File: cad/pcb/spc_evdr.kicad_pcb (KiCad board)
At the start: 2 copper layers, 199.5 x 100.5 mm, 93 parts, among them J1 BL_CONN, SW1 SW_Push, SW10 SW_Push, SW11 SW_Push, SW12 SW_Push, SW13 ON_OFF, SW14 SW_Push, SW15 SW_Push, SW16 SW_Push, SW17 SW_Push, SW18 SW_Push, SW19 SW_Push, SW2 SW_Push, SW20 SW_Push, SW21 SW_Push, SW22 SW_Push, SW23 SW_Push, SW24 SW_Push, SW25 SW_Push, SW26 SW_Push, SW27 SW_Push, SW28 SW_Push, SW29 SW_Push, SW3 SW_Push, SW30 SW_Push, SW31 SW_Push, SW32 SW_Push, SW33 SW_Push, SW34 SW_Push, SW35 SW_Push, SW36 SW_Push, SW37 SW_Push, SW38 SW_Push, SW39 SW_Push, SW4 SW_Push, SW40 SW_Push, SW41 SW_Push, SW42 SW_Push, SW43 SW_Push, SW44 SW_Push, SW45 SW_Push, SW5 RotaryEncoder_Switch, SW6 SW_Push, SW7 SW_Push, SW8 SW_Push, SW9 SW_Push, U1 PCA9555PW, U2 xiao-ble

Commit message: added a whole lot of peripherals
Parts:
- added BZ1: Buzzer, KLOR:Buzzer_Mallory_AST1109MLTRQ_reversible, B.Cu at (85.7, 49.7)
- added D1: D, weteor:D_SOD-123, B.Cu at (48.8, 75.7)
- added D11: D, weteor:D_SOD-123, B.Cu at (222.6, 75.7)
- added D13: D, weteor:D_SOD-123, B.Cu at (48.8, 94.7)
- added D23: D, weteor:D_SOD-123, B.Cu at (222.6, 94.7)
- added D25: D, weteor:D_SOD-123, B.Cu at (48.8, 113.8)
- added D35: D, weteor:D_SOD-123, B.Cu at (222.6, 113.8)
- added D37: D, weteor:D_SOD-123, B.Cu at (48.8, 132.8)
- added D46: D, weteor:D_SOD-123, B.Cu at (231.0, 132.8)
- added D48: ~, weteor:D_SOD-123, F.Cu at (244.0, 131.5)
- added D49: ~, weteor:D_SOD-123, F.Cu at (251.0, 131.5)
- added D50: ~, weteor:D_SOD-123, F.Cu at (255.5, 131.7)
- added D51: ~, weteor:D_SOD-123, F.Cu at (245.0, 115.5)
- added D52: ~, weteor:D_SOD-123, F.Cu at (254.5, 115.5)
- added L1: SK6812MINI, LED_SMD:LED_SK6812MINI_PLCC4_3.5x3.5mm_P1.75mm, F.Cu at (242.1, 47.0)
- added L2: SK6812MINI, LED_SMD:LED_SK6812MINI_PLCC4_3.5x3.5mm_P1.75mm, F.Cu at (250.1, 47.0)
- added L3: SK6812MINI, LED_SMD:LED_SK6812MINI_PLCC4_3.5x3.5mm_P1.75mm, F.Cu at (258.1, 47.0)
- added SW1: SW_Push, weteor:CherryMX_Hotswap, F.Cu at (40.5, 66.2)
- added SW12: SW_Push, weteor:CherryMX_Hotswap, F.Cu at (231.0, 66.2)
- added SW15: SW_Push, weteor:CherryMX_Hotswap, F.Cu at (40.5, 85.2)
- added SW25: SW_Push, weteor:CherryMX_Hotswap, F.Cu at (231.0, 85.2)
- added SW27: SW_Push, weteor:CherryMX_Hotswap, F.Cu at (40.5, 104.3)
- added SW37: SW_Push, weteor:CherryMX_Hotswap, F.Cu at (231.0, 104.3)
- added SW39: SW_Push, weteor:CherryMX_Hotswap, F.Cu at (40.5, 123.3)
- added SW47: SW_Push, weteor:CherryMX_Hotswap, F.Cu at (231.0, 123.3)
- added SW54: SKRHAAE010, mouser:SKRHAAE010, F.Cu at (250.0, 123.3)
- added U3: Pimoroni haptic buzz, KLOR:Pimoroni Haptic Buzz DRV2605L Driver, B.Cu at (202.0, 53.5)
- SW10: renamed from SW35; footprint weteor:Inv1_CherryMX_Hotswap -> weteor:CherryMX_Hotswap
- SW11: renamed from SW38; footprint weteor:Inv1_CherryMX_Hotswap -> weteor:CherryMX_Hotswap
- SW14: renamed from SW42; footprint weteor:Inv1_CherryMX_Hotswap -> weteor:CherryMX_Hotswap
- SW16: renamed from SW2; footprint weteor:Inv1_CherryMX_Hotswap -> weteor:CherryMX_Hotswap
- SW17: renamed from SW7; footprint weteor:Inv1_CherryMX_Hotswap -> weteor:CherryMX_Hotswap
- SW18: renamed from SW11; footprint weteor:Inv1_CherryMX_Hotswap -> weteor:CherryMX_Hotswap
- SW19: renamed from SW15; footprint weteor:Inv1_CherryMX_Hotswap -> weteor:CherryMX_Hotswap
- SW2: renamed from SW1; footprint weteor:Inv1_CherryMX_Hotswap -> weteor:CherryMX_Hotswap
- SW20: renamed from SW21; footprint weteor:Inv1_CherryMX_Hotswap -> weteor:CherryMX_Hotswap
- SW21: renamed from SW26; footprint weteor:Inv1_CherryMX_Hotswap -> weteor:CherryMX_Hotswap
- SW22: renamed from SW32; footprint weteor:Inv1_CherryMX_Hotswap -> weteor:CherryMX_Hotswap
- SW23: renamed from SW36; footprint weteor:Inv1_CherryMX_Hotswap -> weteor:CherryMX_Hotswap
- SW24: renamed from SW39; footprint weteor:Inv1_CherryMX_Hotswap -> weteor:CherryMX_Hotswap
- SW26: renamed from SW43; footprint weteor:Inv1_CherryMX_Hotswap -> weteor:CherryMX_Hotswap
- SW28: renamed from SW3; footprint weteor:Inv1_CherryMX_Hotswap -> weteor:CherryMX_Hotswap
- SW29: renamed from SW8; footprint weteor:Inv1_CherryMX_Hotswap -> weteor:CherryMX_Hotswap
- SW3: renamed from SW6; footprint weteor:Inv1_CherryMX_Hotswap -> weteor:CherryMX_Hotswap
- SW30: renamed from SW12; footprint weteor:Inv1_CherryMX_Hotswap -> weteor:CherryMX_Hotswap
- SW31: renamed from SW16; footprint weteor:Inv1_CherryMX_Hotswap -> weteor:CherryMX_Hotswap
- SW32: renamed from SW22; footprint weteor:Inv1_CherryMX_Hotswap -> weteor:CherryMX_Hotswap
- SW33: renamed from SW27; footprint weteor:Inv1_CherryMX_Hotswap -> weteor:CherryMX_Hotswap
- SW34: renamed from SW33; footprint weteor:Inv1_CherryMX_Hotswap -> weteor:CherryMX_Hotswap
- SW35: renamed from SW37; footprint weteor:Inv1_CherryMX_Hotswap -> weteor:CherryMX_Hotswap
- SW36: renamed from SW40; footprint weteor:Inv1_CherryMX_Hotswap -> weteor:CherryMX_Hotswap
- SW38: renamed from SW44; footprint weteor:Inv1_CherryMX_Hotswap -> weteor:CherryMX_Hotswap
- SW4: renamed from SW10; footprint weteor:Inv1_CherryMX_Hotswap -> weteor:CherryMX_Hotswap
- SW40: renamed from SW4; footprint weteor:Inv1_CherryMX_Hotswap -> weteor:CherryMX_Hotswap
- SW41: renamed from SW9; footprint weteor:Inv1_CherryMX_Hotswap -> weteor:CherryMX_Hotswap
- SW42: renamed from SW17; footprint weteor:Inv1_CherryMX_Hotswap -> weteor:CherryMX_Hotswap
- SW43: renamed from SW23; footprint weteor:Inv_CherryMX_Hotswap_1.75u -> weteor:CherryMX_Hotswap_1.75u
- SW44: renamed from SW28; footprint weteor:Inv_CherryMX_Hotswap_1.75u -> weteor:CherryMX_Hotswap_1.75u
- SW45: renamed from SW34; footprint weteor:Inv1_CherryMX_Hotswap -> weteor:CherryMX_Hotswap
- SW46: renamed from SW41; footprint weteor:Inv1_CherryMX_Hotswap -> weteor:CherryMX_Hotswap
- SW48: renamed from SW45; footprint weteor:Inv1_CherryMX_Hotswap -> weteor:CherryMX_Hotswap
- SW49: renamed from SW18; footprint weteor:Inv_CherryMX_Hotswap_1.25u -> weteor:CherryMX_Hotswap_1.25u
- SW5: footprint weteor:ec11_smd -> KLOR:RotaryEncoder_Alps_EC11E-Switch_Vertical_H20mm-keebio_modified
- SW50: renamed from SW24; footprint weteor:InvCherryMX_Hotswap_3u_stabs -> weteor:CherryMX_Hotswap_3u_stabs
- SW51: renamed from SW29; footprint weteor:Inv_CherryMX_Hotswap_1.25u -> weteor:CherryMX_Hotswap_1.25u
- SW52: renamed from SW19; footprint weteor:InvCherryMX_Hotswap_2.25u_stabs -> weteor:CherryMX_Hotswap_2.25u_stabs
- SW53: renamed from SW30; footprint weteor:InvCherryMX_Hotswap_2.25u_stabs -> weteor:CherryMX_Hotswap_2.25u_stabs
- SW6: renamed from SW14; footprint weteor:Inv1_CherryMX_Hotswap -> weteor:CherryMX_Hotswap
- SW7: renamed from SW20; footprint weteor:Inv1_CherryMX_Hotswap -> weteor:CherryMX_Hotswap
- SW8: renamed from SW25; footprint weteor:Inv1_CherryMX_Hotswap -> weteor:CherryMX_Hotswap
- SW9: renamed from SW31; footprint weteor:Inv1_CherryMX_Hotswap -> weteor:CherryMX_Hotswap
- moved D39 69.5 mm to (46.4, 53.3), turned to 180 degrees
- moved D12 35.3 mm to (241.7, 75.7)
- moved D24 35.3 mm to (241.7, 94.7)
- moved D36 35.3 mm to (241.7, 113.8)
- moved SW48 35.3 mm to (250.0, 123.3)
- moved SW14 35.3 mm to (250.0, 66.2)
- moved SW26 35.3 mm to (250.0, 85.2)
- moved D47 35.3 mm to (250.0, 132.8)
- moved SW38 35.3 mm to (250.0, 104.3)
- moved OL1 35.3 mm to (264.1, 47.3)
- moved SW5 32.6 mm to (38.0, 46.7), turned to 180 degrees
- moved D41 28.2 mm to (134.5, 137.6)
- moved D42 28.2 mm to (136.9, 137.6)
- moved D43 28.2 mm to (153.6, 137.6)
- moved D44 28.2 mm to (156.0, 137.6)
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- renumbered D31 to D10, D35 to D12, D2 to D14, D7 to D15, D10 to D16, D13 to D17, D17 to D18, D21 to D19, D1 to D2, D25 to D20, D29 to D21, D32 to D22, D36 to D24, D3 to D26, D8 to D27, D11 to D28, D14 to D29, D6 to D3, D18 to D30, D22 to D31, D26 to D32, D30 to D33, D33 to D34, D37 to D36, D4 to D38, D9 to D4, D5 to D40, D15 to D41, D19 to D42, D23 to D43, D27 to D44, D34 to D45, D38 to D47, D12 to D5, D16 to D6, D20 to D7, D24 to D8, D28 to D9
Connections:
- SW14 pad 1: Col_10 -> Col_11
- SW26 pad 1: Col_10 -> Col_11
- SW38 pad 1: Col_10 -> Col_11
- SW48 pad 1: Col_10 -> Col_11
- U1 pad 13: unconnected-(U1-Pad13) -> Col_5
- U1 pad 14: unconnected-(U1-Pad14) -> Col_11
- U1 pad 17: unconnected-(U1-Pad17) -> Col_9
- U1 pad 19: unconnected-(U1-Pad19) -> Col_10
- U1 pad 8: Col_5 -> Col_0
- U2 pad 14: unconnected-(U2-Pad14) -> +5V
- U2 pad 3: unconnected-(U2-Pad3) -> LED
- U2 pad 4: Col_10 -> Row_0
- U2 pad 7: Col_9 -> AUDIO
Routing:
- net Col_11: track 0.00 -> 214.5 mm, vias 0 -> 7
- net Row_0: track 0.00 -> 165.8 mm, vias 0 -> 9
- net Col_0: track 0.00 -> 164.9 mm, vias 0 -> 8
- net +5V: track 0.00 -> 146.9 mm, vias 0 -> 3
- net Row_4: track 292.9 -> 387.0 mm
- net LED: track 0.00 -> 91.8 mm, vias 0 -> 3
- net AUDIO: track 0.00 -> 66.3 mm, vias 0 -> 3
- net sda: track 135.1 -> 199.9 mm, vias 2 -> 4
- net Net-(D39-A): track 63.5 -> 16.0 mm
- net Row_2: track 200.8 -> 238.9 mm
- net Row_3: track 223.2 -> 261.3 mm
- net Row_1: track 221.9 -> 260.0 mm
- net scl: track 138.9 -> 167.7 mm, vias 4 -> 3
- net Col_9: track 141.2 -> 164.2 mm, vias 5 -> 7
- net +3V3: track 172.2 -> 192.6 mm
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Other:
- board size 199.5 x 100.5 mm -> 237.6 x 100.5 mm

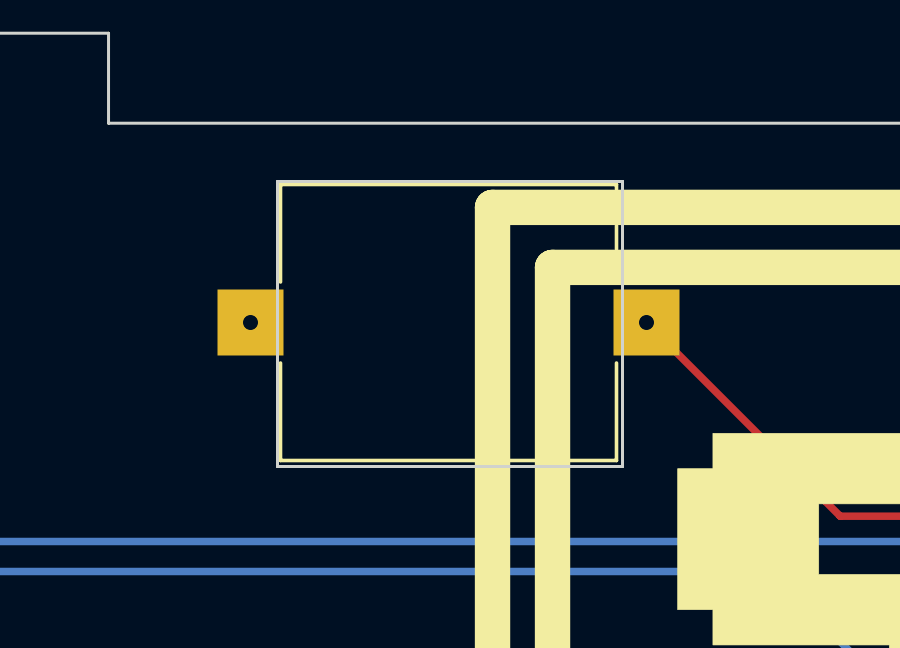
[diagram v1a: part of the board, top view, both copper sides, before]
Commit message: fix wire disconnect in matrix
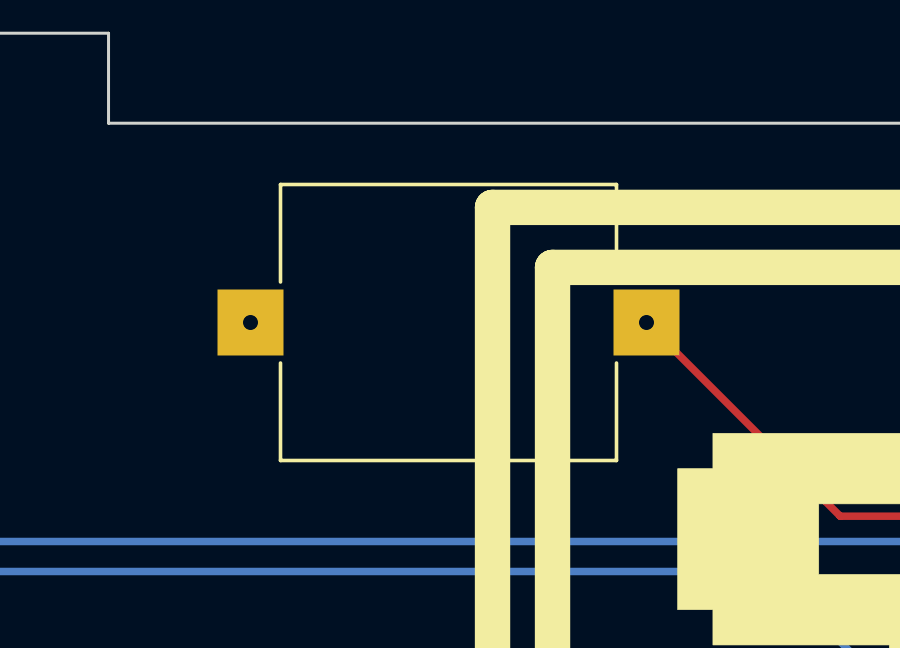
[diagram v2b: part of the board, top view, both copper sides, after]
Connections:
- D1 pad 1: unconnected-(D1-K-Pad1) -> Row_1
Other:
- outline, holes or cut-outs redrawn

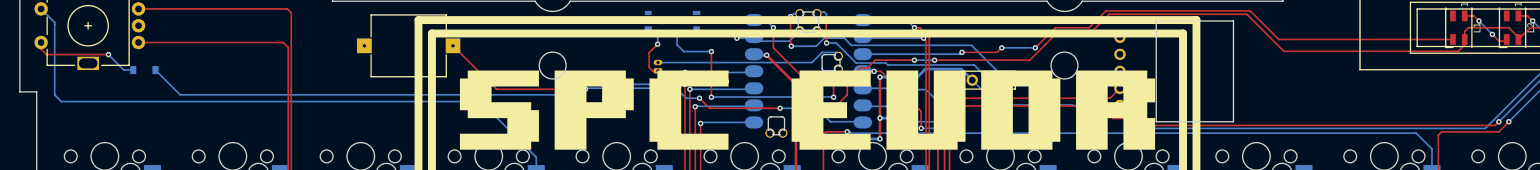
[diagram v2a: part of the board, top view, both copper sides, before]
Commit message: track nudging
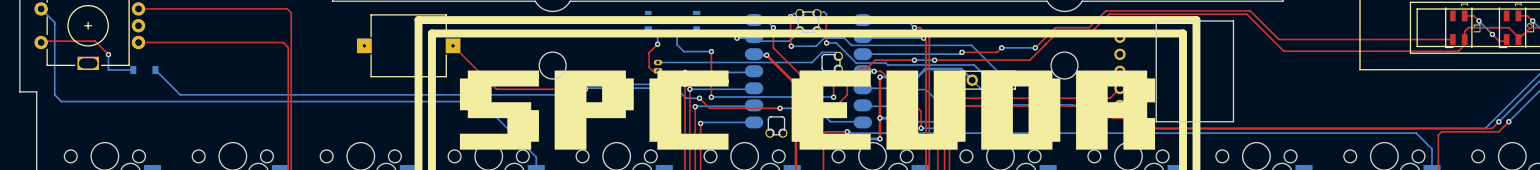
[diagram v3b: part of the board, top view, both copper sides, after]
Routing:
- net Net-(D39-A): track 16.0 -> 16.9 mm
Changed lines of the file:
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@@
   (segment (start 143.367689 63.55719) (end 143.367689 55.454879) (width 0.4) (layer "F.Cu") (net 4))
   (segment (start 155.867689 60.45719) (end 155.867689 63.55719) (width 0.4) (layer "F.Cu") (net 4))
-  (segment (start 143.367689 63.55719) (end 143.367689 69.65719) (width 0.4) (layer "F.Cu") (net 4))
   (segment (start 145.667689 71.95719) (end 145.667689 74.85719) (width 0.4) (layer "F.Cu") (net 4))
+  (segment (start 143.367689 69.65719) (end 145.667689 71.95719) (width 0.4) (layer "F.Cu") (net 4))
   (segment (start 143.367689 55.454879) (end 139 51.08719) (width 0.4) (layer "F.Cu") (net 4))
   (segment (start 155.867689 54.35719) (end 155.867689 60.45719) (width 0.4) (layer "F.Cu") (net 4))
   (segment (start 150.967689 82.85719) (end 152.367689 81.45719) (width 0.4) (layer "F.Cu") (net 4))
   (segment (start 150.367689 82.85719) (end 150.967689 82.85719) (width 0.4) (layer "F.Cu") (net 4))
-  (segment (start 143.367689 69.65719) (end 145.667689 71.95719) (width 0.4) (layer "F.Cu") (net 4))
+  (segment (start 143.367689 63.55719) (end 143.367689 69.65719) (width 0.4) (layer "F.Cu") (net 4))
   (via (at 150.367689 82.85719) (size 0.8) (drill 0.4) (layers "F.Cu" "B.Cu") (net 4))
   (via (at 155.867689 63.55719) (size 0.8) (drill 0.4) (layers "F.Cu" "B.Cu") (net 4))
@@
   (segment (start 164 57.5) (end 162.71969 56.21969) (width 0.25) (layer "B.Cu") (net 40))
   (segment (start 147.980189 82.23219) (end 149.392689 82.23219) (width 0.25) (layer "B.Cu") (net 40))
-  (segment (start 247.474598 61.55) (end 195.05 61.55) (width 0.25) (layer "F.Cu") (net 41))
   (segment (start 165.5 58.665001) (end 165.492189 58.65719) (width 0.25) (layer "F.Cu") (net 41))
   (segment (start 193 60.5) (end 193.5 60) (width 0.25) (layer "F.Cu") (net 41))
   (segment (start 165.492189 58.65719) (end 188.65719 58.65719) (width 0.25) (layer "F.Cu") (net 41))
+  (segment (start 248.012299 61.012299) (end 247.024598 62) (width 0.25) (layer "F.Cu") (net 41))
   (segment (start 193.5 55.4) (end 191.6 53.5) (width 0.25) (layer "F.Cu") (net 41))
   (segment (start 165.492189 78.653478) (end 165.492189 58.65719) (width 0.25) (layer "F.Cu") (net 41))
+  (segment (start 195.5 62) (end 193.5 60) (width 0.25) (layer "F.Cu") (net 41))
   (segment (start 193.5 60) (end 193.5 55.4) (width 0.25) (layer "F.Cu") (net 41))
   (segment (start 188.65719 58.65719) (end 190.5 60.5) (width 0.25) (layer "F.Cu") (net 41))
-  (segment (start 195.05 61.55) (end 193.5 60) (width 0.25) (layer "F.Cu") (net 41))
-  (segment (start 248.012299 61.012299) (end 247.474598 61.55) (width 0.25) (layer "F.Cu") (net 41))
+  (segment (start 247.024598 62) (end 195.5 62) (width 0.25) (layer "F.Cu") (net 41))
   (segment (start 165.5 61) (end 165.5 58.665001) (width 0.25) (layer "F.Cu") (net 41))
   (segment (start 190.5 60.5) (end 193 60.5) (width 0.25) (layer "F.Cu") (net 41))
@@
   (segment (start 53.700689 130.39019) (end 54.367689 131.05719) (width 0.25) (layer "B.Cu") (net 60))
   (segment (start 54.367689 131.05719) (end 59.542689 131.05719) (width 0.25) (layer "B.Cu") (net 60))
-  (segment (start 31.770499 51) (end 30.977689 50.20719) (width 0.25) (layer "F.Cu") (net 61))
-  (segment (start 30.977689 50.20719) (end 30.977689 49.20719) (width 0.25) (layer "F.Cu") (net 61))
-  (segment (start 31.770499 51) (end 41 51) (width 0.25) (layer "F.Cu") (net 61))
+  (segment (start 39 49) (end 41 51) (width 0.25) (layer "F.Cu") (net 61))
+  (segment (start 30.977689 49.20719) (end 31.184879 49) (width 0.25) (layer "F.Cu") (net 61))
+  (segment (start 31.184879 49) (end 39 49) (width 0.25) (layer "F.Cu") (net 61))
   (via (at 41 51) (size 0.8) (drill 0.4) (layers "F.Cu" "B.Cu") (net 61))
-  (segment (start 43.30719 53.30719) (end 44.7 53.30719) (width 0.25) (layer "B.Cu") (net 61))
-  (segment (start 41 51) (end 43.30719 53.30719) (width 0.25) (layer "B.Cu") (net 61))
+  (segment (start 41 51) (end 41 53.30719) (width 0.25) (layer "B.Cu") (net 61))
+  (segment (start 41 53.30719) (end 44.7 53.30719) (width 0.25) (layer "B.Cu") (net 61))
   (segment (start 72.700689 130.39019) (end 73.367689 131.05719) (width 0.25) (layer "B.Cu") (net 62))
   (segment (start 72.700689 128.26219) (end 72.700689 130.39019) (width 0.25) (layer "B.Cu") (net 62))
